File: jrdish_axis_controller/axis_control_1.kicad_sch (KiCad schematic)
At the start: 25 parts, among them CN1 KF2EDGR-2.54-9P, CN2 KF2EDGR-2.54-6P

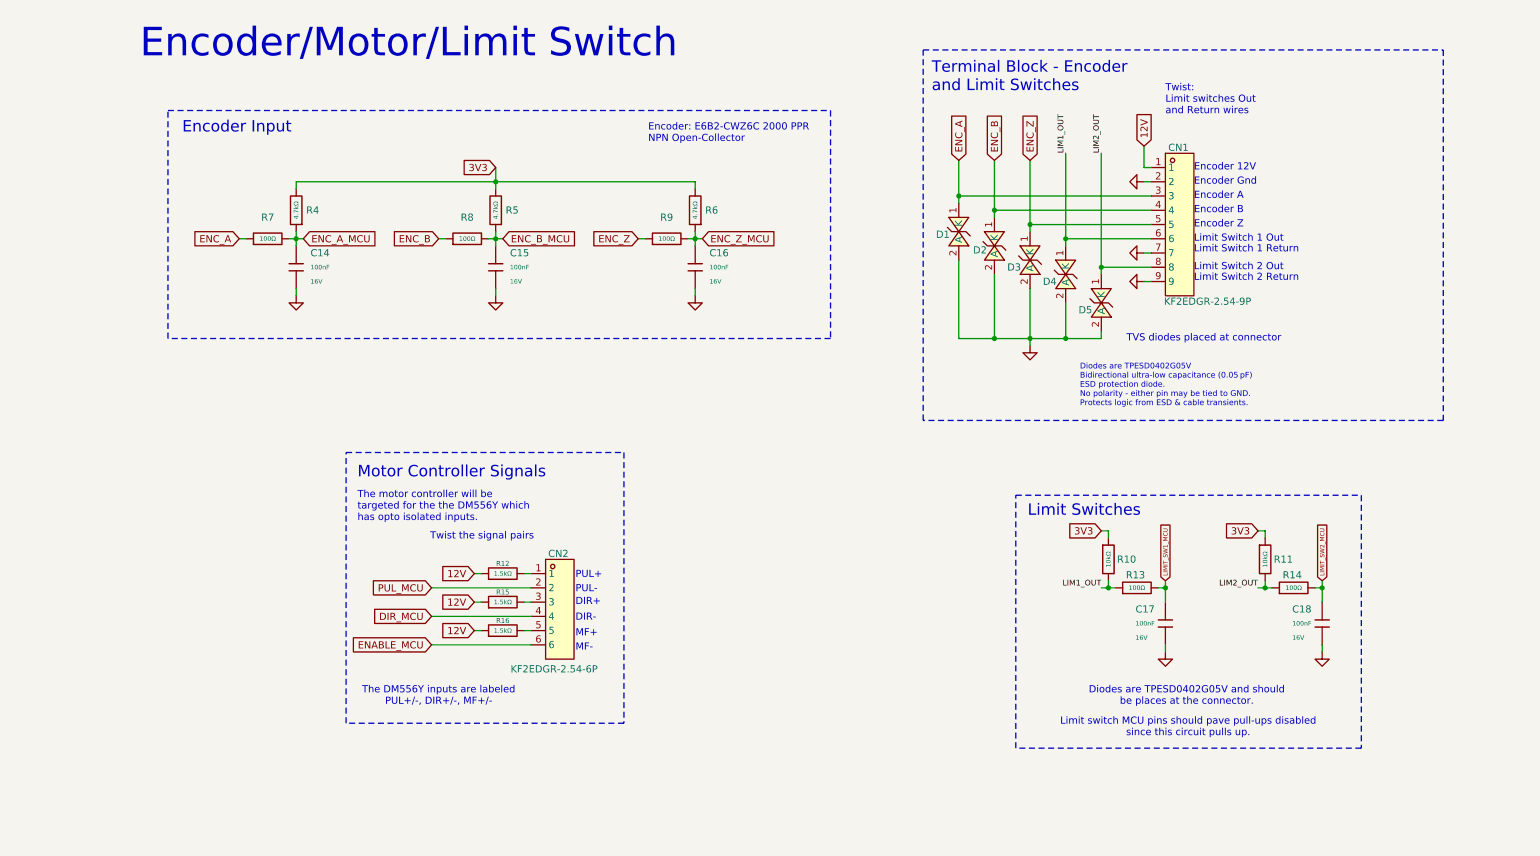
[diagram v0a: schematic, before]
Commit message: New 64pin version - 2 axes
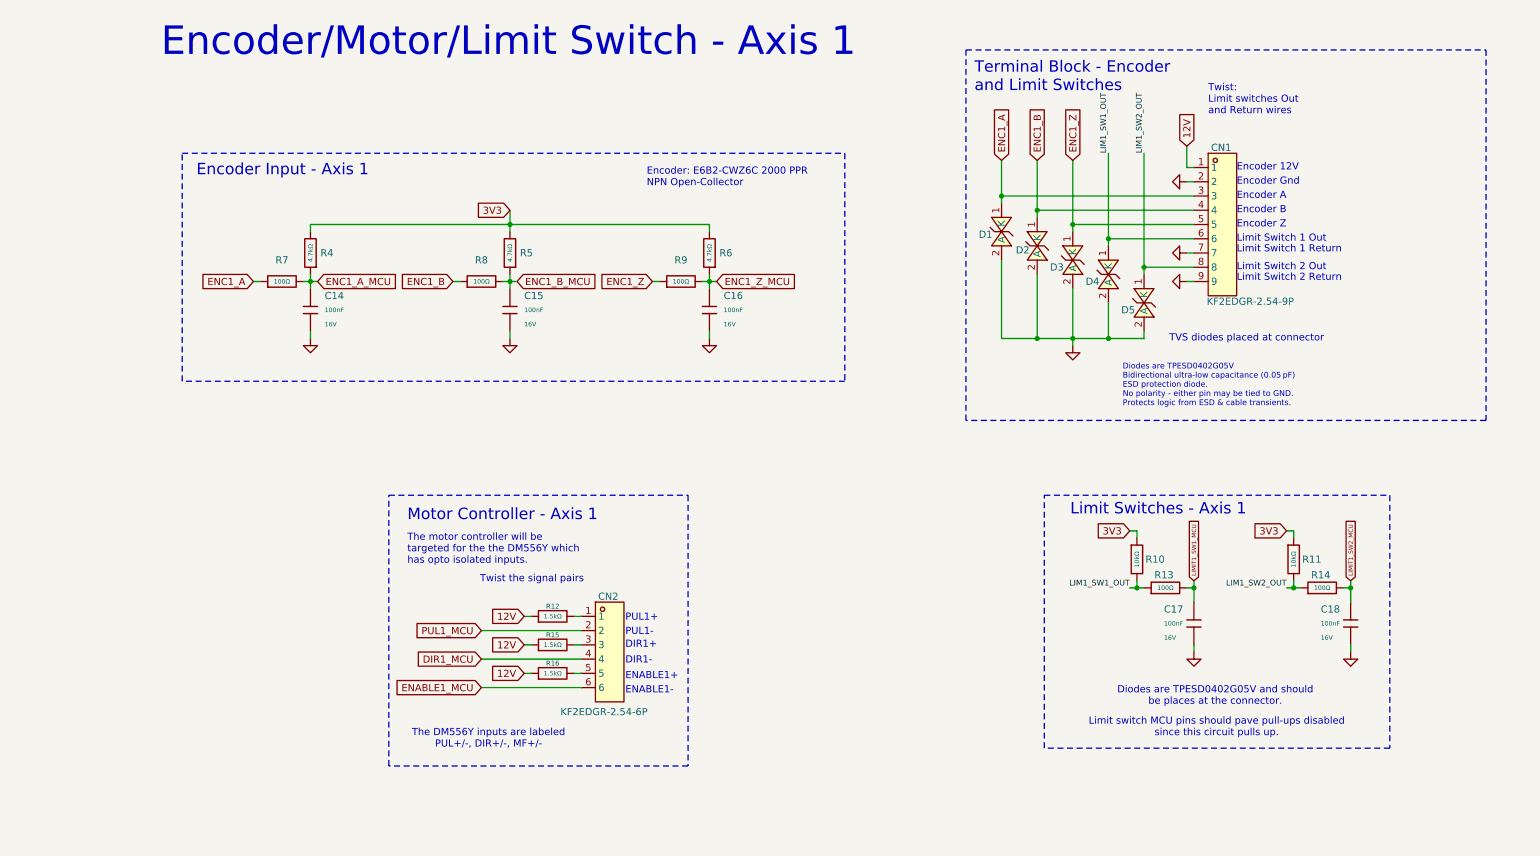
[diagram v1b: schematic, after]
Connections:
- net DIR_MCU renamed DIR1_MCU
- net ENABLE_MCU renamed ENABLE1_MCU
- net ENC_A renamed ENC1_A
- net ENC_A_MCU renamed ENC1_A_MCU
- net ENC_B renamed ENC1_B
- net ENC_B_MCU renamed ENC1_B_MCU
- net ENC_Z renamed ENC1_Z
- net ENC_Z_MCU renamed ENC1_Z_MCU
- net LIM1_OUT renamed LIM1_SW1_OUT
- net LIM2_OUT renamed LIM1_SW2_OUT
- net LIMIT_SW1_MCU renamed LIMIT1_SW1_MCU
- net LIMIT_SW2_MCU renamed LIMIT1_SW2_MCU
- net PUL_MCU renamed PUL1_MCU
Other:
- note added: "DIR1+"
- note added: "DIR1-"
- note added: "ENABLE1+"
- note added: "ENABLE1-"
- note added: "Encoder Input - Axis 1"
- note added: "Encoder/Motor/Limit Switch - Axis 1"
- note added: "Limit Switches - Axis 1"
- note added: "Motor Controller - Axis 1"
- note added: "PUL1+"
- note added: "PUL1-"
- note removed: "DIR+"
- note removed: "DIR-"
- note removed: "Encoder Input"
- note removed: "Encoder/Motor/Limit Switch"
- note removed: "Limit Switches"
- note removed: "MF+"
- note removed: "MF-"
- note removed: "Motor Controller Signals"
- note removed: "PUL+"
- note removed: "PUL-"
- moved on the sheet: C14, C15, C16, C17, C18, CN1, CN2, D1, D2, D3, D4, D5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

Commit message: Continuing layout
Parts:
- removed R12, R15, R16: 1.5kΩ, PCM_JLCPCB:R_0402, symbol PCM_JLCPCB-Resistors:0402,1.5kΩ
- added R14, R15, R16: 330Ω, PCM_JLCPCB:R_0402, symbol PCM_JLCPCB-Resistors:0402,330Ω
- renumbered C14 to C15, C15 to C16, C16 to C17, C17 to C18, C18 to C19, R13 to R12, R14 to R13
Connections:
- net 3V3: now also R14.1, R15.1, R16.1
- net at CN2.3: now also R15.2
- net at CN2.1: now also R14.2
- net at CN2.5: now also R16.2

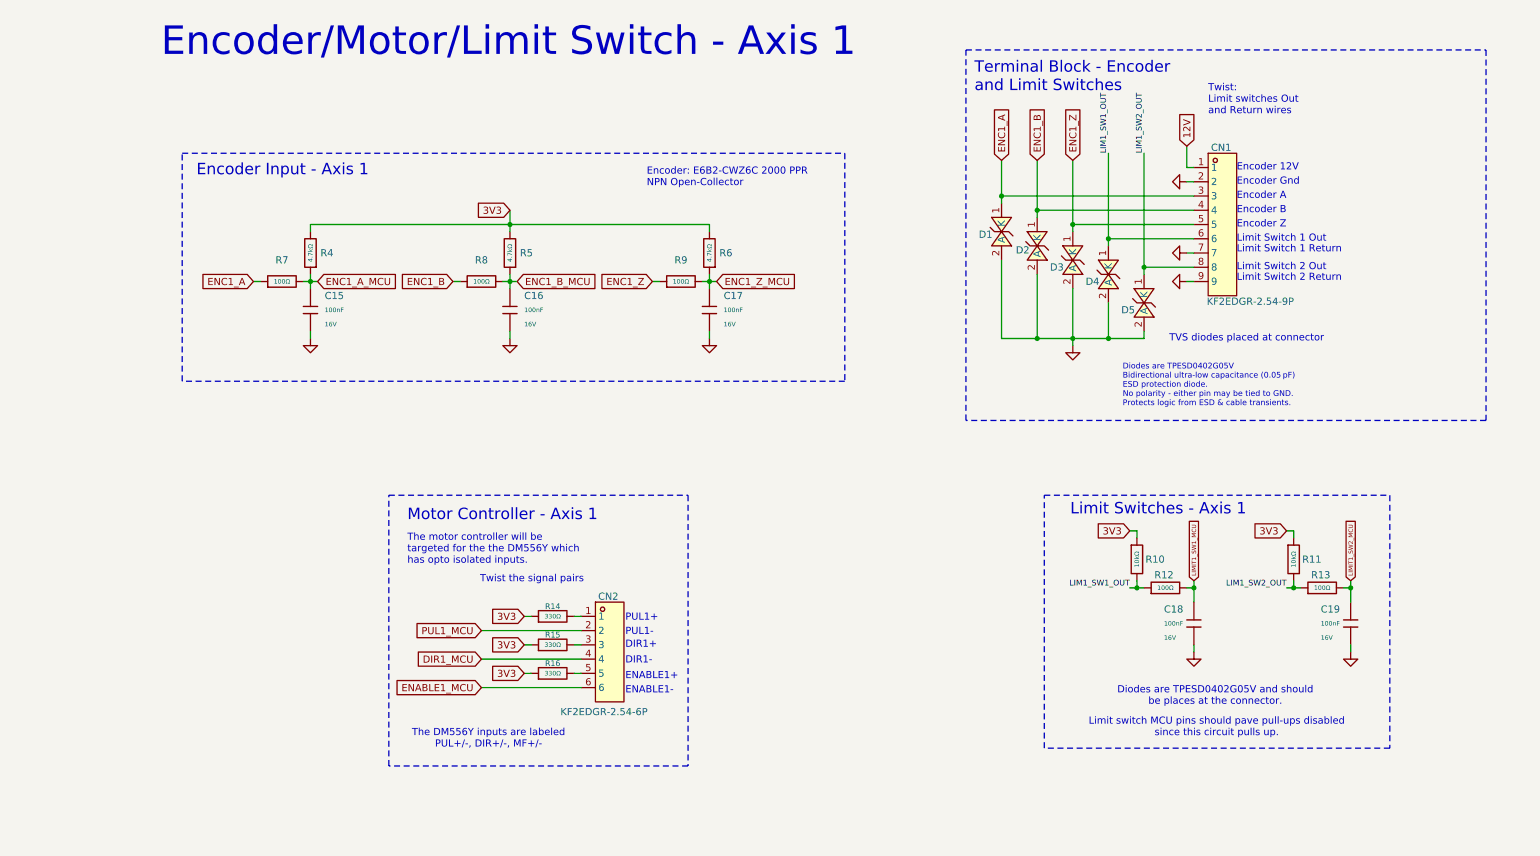
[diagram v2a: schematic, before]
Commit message: RS485 isolated areas in place
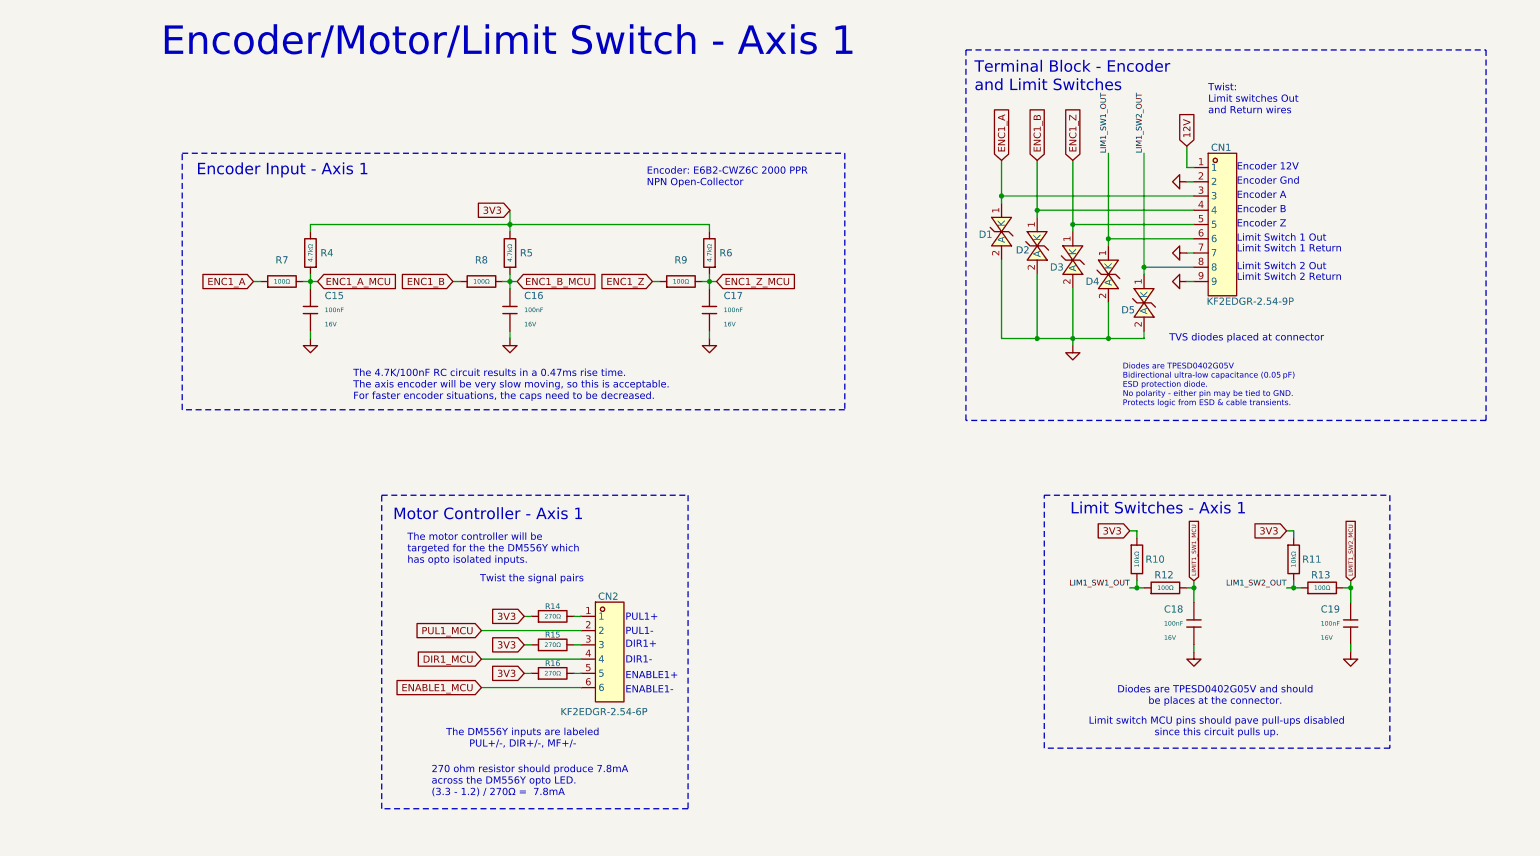
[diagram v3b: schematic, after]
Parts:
- removed R14, R15, R16: 330Ω, PCM_JLCPCB:R_0402, symbol PCM_JLCPCB-Resistors:0402,330Ω
- added R14, R15, R16: 270Ω, PCM_JLCPCB:R_0603, symbol PCM_JLCPCB-Resistors:0603,270Ω
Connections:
- net 3V3: now also R14.1, R15.1, R16.1
- net at CN2.3: now also R15.2
- net at CN2.5: now also R16.2
- net at CN2.1: now also R14.2
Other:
- note added: "270 ohm resistor should produce 7.8mA across the DM556Y opto LED. (3.3 - 1.2) / 270Ω = 7.8mA"
- note added: "The 4.7K/100nF RC circuit results in a 0.47ms rise time. The axis encoder will be very slow moving, so this is acceptable. For faster encoder situations, the caps need to be decreased."

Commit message: Layout complete
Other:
- note added: "Diodes are TPESD0402G05V Bidirectional ultra-low capacitance (0.05 pF) ESD protection diode. No polarity - either pin may be tied to GND. Protects logic from ESD & cable transients. E6B2-CWZ6C NPN Open-collector Output Model."
- note removed: "Diodes are TPESD0402G05V Bidirectional ultra-low capacitance (0.05 pF) ESD protection diode. No polarity - either pin may be tied to GND. Protects logic from ESD & cable transients."
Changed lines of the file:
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@@
 		)
 	)
-	(text "Diodes are TPESD0402G05V\nBidirectional ultra-low capacitance (0.05 pF) \nESD protection diode.\nNo polarity - either pin may be tied to GND.\nProtects logic from ESD & cable transients."
+	(text "Diodes are TPESD0402G05V\nBidirectional ultra-low capacitance (0.05 pF) \nESD protection diode.\nNo polarity - either pin may be tied to GND.\nProtects logic from ESD & cable transients.\nE6B2-CWZ6C NPN Open-collector Output Model."
 		(exclude_from_sim no)
 		(at 198.12 80.772 0)
@@
 	)
 	(symbol
+		(lib_name "TPESD0402G05V_4")
 		(lib_id "MyParts:TPESD0402G05V")
 		(at 182.88 55.88 270)
@@
 			)
 		)
-		(property "Datasheet" ""
+		(property "Datasheet" "https://www.lcsc.com/datasheet/C558615.pdf?spm=wm.sxq.inf.ggs___wm.ssy.bg.0.xh&lcsc_vid=FFBaV1wHQFldUVICFgBfBVJTQVJWXgBfEQRYBAFQE1YxVlNRQFVXU1JRQVReUTsOAxUeFF5JWBYZEEoKFBINSQcJGk4eFQsCAgIaSgADAwAHC0slRldcU1ZUWQkaCgg%3D"
 			(at 182.88 55.88 0)
 			(hide yes)
@@
 			)
 		)
-		(property "Description" ""
+		(property "Description" "5VWM 40VC 0402"
 			(at 182.88 55.88 0)
+			(hide yes)
 			(show_name no)
 			(do_not_autoplace no)
@@
 			)
 		)
-		(property "Datasheet" ""
+		(property "Datasheet" "https://www.lcsc.com/datasheet/C558615.pdf?spm=wm.sxq.inf.ggs___wm.ssy.bg.0.xh&lcsc_vid=FFBaV1wHQFldUVICFgBfBVJTQVJWXgBfEQRYBAFQE1YxVlNRQFVXU1JRQVReUTsOAxUeFF5JWBYZEEoKFBINSQcJGk4eFQsCAgIaSgADAwAHC0slRldcU1ZUWQkaCgg%3D"
 			(at 189.23 58.42 0)
 			(hide yes)
@@
 			)
 		)
-		(property "Description" ""
+		(property "Description" "5VWM 40VC 0402"
 			(at 189.23 58.42 0)
+			(hide yes)
 			(show_name no)
 			(do_not_autoplace no)
@@
 	)
 	(symbol
+		(lib_name "TPESD0402G05V_1")
 		(lib_id "MyParts:TPESD0402G05V")
 		(at 201.93 66.04 270)
@@
 			)
 		)
-		(property "Datasheet" ""
+		(property "Datasheet" "https://www.lcsc.com/datasheet/C558615.pdf?spm=wm.sxq.inf.ggs___wm.ssy.bg.0.xh&lcsc_vid=FFBaV1wHQFldUVICFgBfBVJTQVJWXgBfEQRYBAFQE1YxVlNRQFVXU1JRQVReUTsOAxUeFF5JWBYZEEoKFBINSQcJGk4eFQsCAgIaSgADAwAHC0slRldcU1ZUWQkaCgg%3D"
 			(at 201.93 66.04 0)
 			(hide yes)
@@
 			)
 		)
-		(property "Description" ""
+		(property "Description" "5VWM 40VC 0402"
 			(at 201.93 66.04 0)
+			(hide yes)
 			(show_name no)
 			(do_not_autoplace no)
@@
 	)
 	(symbol
+		(lib_name "TPESD0402G05V_3")
 		(lib_id "MyParts:TPESD0402G05V")
 		(at 176.53 53.34 270)
@@
 			)
 		)
-		(property "Datasheet" ""
+		(property "Datasheet" "https://www.lcsc.com/datasheet/C558615.pdf?spm=wm.sxq.inf.ggs___wm.ssy.bg.0.xh&lcsc_vid=FFBaV1wHQFldUVICFgBfBVJTQVJWXgBfEQRYBAFQE1YxVlNRQFVXU1JRQVReUTsOAxUeFF5JWBYZEEoKFBINSQcJGk4eFQsCAgIaSgADAwAHC0slRldcU1ZUWQkaCgg%3D"
 			(at 176.53 53.34 0)
 			(hide yes)
@@
 			)
 		)
-		(property "Description" ""
+		(property "Description" "5VWM 40VC 0402"
 			(at 176.53 53.34 0)
+			(hide yes)
 			(show_name no)
 			(do_not_autoplace no)
@@
 	)
 	(symbol
+		(lib_name "TPESD0402G05V_2")
 		(lib_id "MyParts:TPESD0402G05V")
 		(at 195.58 60.96 270)
@@
 			)
 		)
-		(property "Datasheet" ""
+		(property "Datasheet" "https://www.lcsc.com/datasheet/C558615.pdf?spm=wm.sxq.inf.ggs___wm.ssy.bg.0.xh&lcsc_vid=FFBaV1wHQFldUVICFgBfBVJTQVJWXgBfEQRYBAFQE1YxVlNRQFVXU1JRQVReUTsOAxUeFF5JWBYZEEoKFBINSQcJGk4eFQsCAgIaSgADAwAHC0slRldcU1ZUWQkaCgg%3D"
 			(at 195.58 60.96 0)
 			(hide yes)
@@
 			)
 		)
-		(property "Description" ""
+		(property "Description" "5VWM 40VC 0402"
 			(at 195.58 60.96 0)
+			(hide yes)
 			(show_name no)
 			(do_not_autoplace no)

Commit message: Making refinements
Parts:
- added D18, D19, D20: TPESD0402G05V, MyParts:D0402-BI, symbol MyParts:TPESD0402G05V
- added R57, R58, R59: 100Ω, PCM_JLCPCB:R_0402, symbol PCM_JLCPCB-Resistors:0402,100Ω
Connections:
- net DIR1_MCU: now also R58.1; no longer CN2.4
- net ENABLE1_MCU: now also R59.1; no longer CN2.6
- net GND: now also D18.2 (A), D19.2 (A), D20.2 (A)
- net PUL1_MCU: now also R57.1; no longer CN2.2
- new net: CN2.2, D18.1 (K), R57.2
- new net: CN2.6, D20.1 (K), R59.2
- new net: CN2.4, D19.1 (K), R58.2

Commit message: Making refinements
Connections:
- removed net GND: C15.2, C16.2, C17.2, C18.2, C19.2, CN1.2, CN1.7, CN1.9, D1.2 (A), D18.2 (A), D19.2 (A), D2.2 (A), D20.2 (A), D3.2 (A), D4.2 (A), D5.2 (A)
- new net: D1.2 (A), D2.2 (A), D3.2 (A), D4.2 (A), D5.2 (A)
- new net: D18.2 (A), D19.2 (A), D20.2 (A)
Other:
- title: Encoder/Motor/Limit Switch -> Encoder/Motor/Limit Switch - Axis1
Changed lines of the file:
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@@
 	(paper "A4")
 	(title_block
-		(title "Encoder/Motor/Limit Switch")
-		(date "2026-04-12")
+		(title "Encoder/Motor/Limit Switch - Axis1")
+		(date "2026-04-30")
 		(rev "1.0")
 		(company "JRSeti")
